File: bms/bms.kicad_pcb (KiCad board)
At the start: 8 copper layers, 60 x 60 mm, 46 parts, among them J2 3S pack power + cell-tap harn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, Q11 CSD18540Q5B reverse-pack FET A, Q12 CSD18540Q5B reverse-pack FET B, Q701 BSS138 pack protector latch r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, Q703 CSD18540Q5B BQ77915 discharge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, Q704 CSD18540Q5B BQ77915 charge FET, U11 LTC4368IMS-1 bidirectional pa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, U719 BQ7791500PWR autonomous 3S pr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

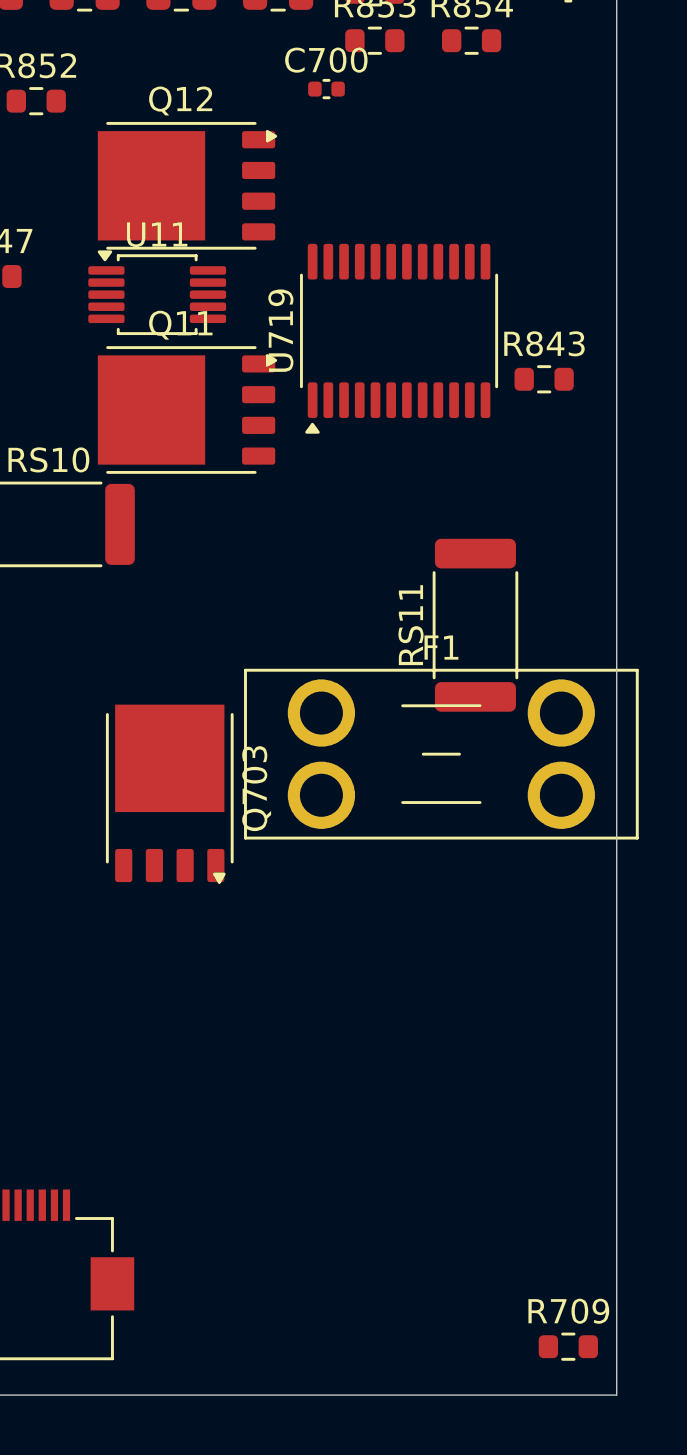
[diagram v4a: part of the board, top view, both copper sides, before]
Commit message: BMS 4-layer + test points + staged bring-up plan
- bms stackup converted from the 8-layer MCP default to a 4-copper
  JLC04161H-style build (1oz, ~1.6mm); In1/In2 are solid FG_VSS return
  planes, pads solid-connected, 2 fills, DRC 0 shorts/clearance/drill
- 16 test points (TPB1-16): every pack rail, protector gate/common,
  fault/retry, rails, gauge shunt sense, FG_VSS scope ground -- in the
  schematic generator AND injected on the board at searched-free spots
  (gen/add_test_points.py, idempotent, reusable per board)
- every differential pair on every board now in an impedance class
  (left USB3 -> DIFF_90, right HDMI/GbE -> DIFF_100, center refclk ->
  DIFF_100); bms pack-current path fully POWER_HI incl. bare FG_VSS
- inherit_netclasses restores rule keys unconditionally + center rules;
  release gate: relocated monolith path, per-board refill staging,
  via_dangling allowed in refill deltas while unrouted
- docs/BRINGUP_TEST_PLAN.md + 4x IPC-D-356 bare-board test netlists;
  verification/FPC_CABLE_SPEC_2026-09-02.md (Type-A cables, lengths,
  purchasing list)
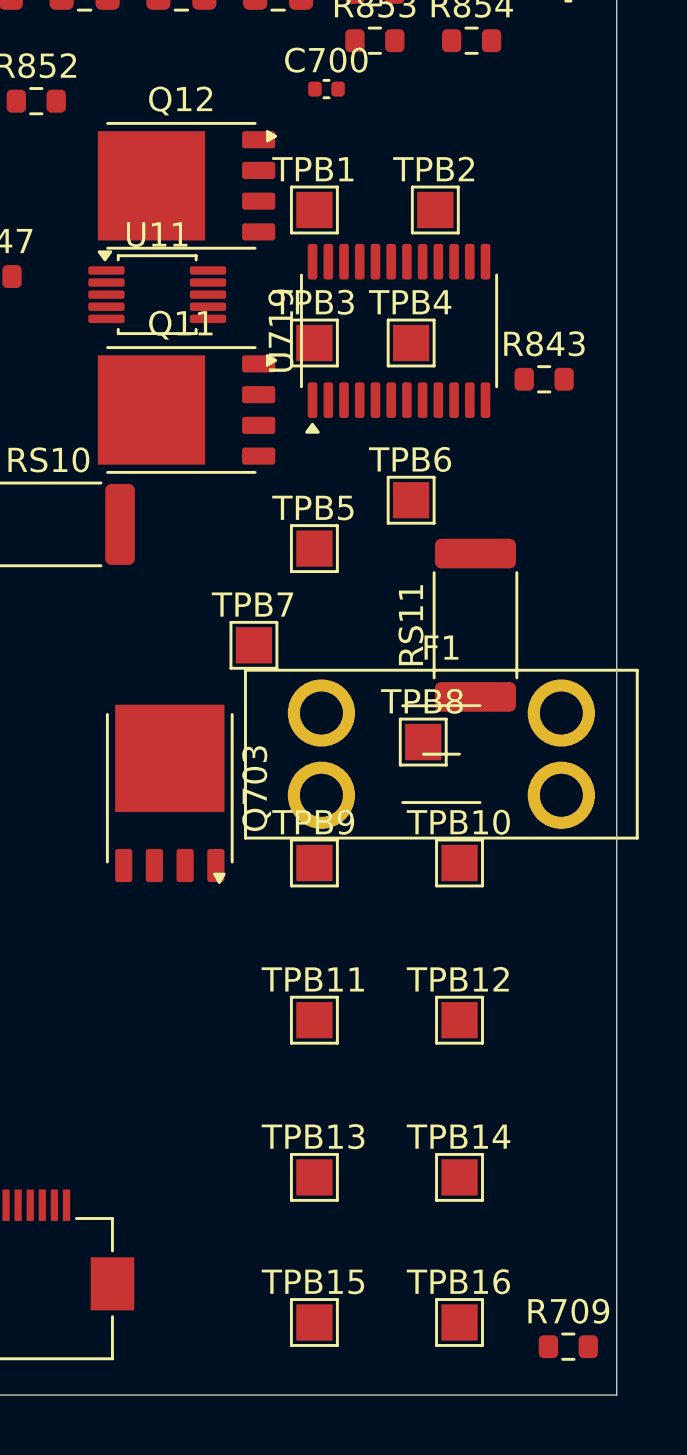
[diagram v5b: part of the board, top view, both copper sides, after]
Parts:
- added TPB1: /PACK_POS_RAW, TestPoint_Pad_1.5x1.5mm, F.Cu at (47.5, 11.0)
- added TPB10: /BMS_AVDD, TestPoint_Pad_1.5x1.5mm, F.Cu at (53.5, 38.0)
- added TPB11: /BMS_VDD, TestPoint_Pad_1.5x1.5mm, F.Cu at (47.5, 44.5)
- added TPB12: /BMS_SRP, TestPoint_Pad_1.5x1.5mm, F.Cu at (53.5, 44.5)
- added TPB13: /BMS_SRN, TestPoint_Pad_1.5x1.5mm, F.Cu at (47.5, 51.0)
- added TPB14: /BMS_PRES, TestPoint_Pad_1.5x1.5mm, F.Cu at (53.5, 51.0)
- added TPB15: /BMS_LD, TestPoint_Pad_1.5x1.5mm, F.Cu at (47.5, 57.0)
- added TPB16: FG_VSS, TestPoint_Pad_1.5x1.5mm, F.Cu at (53.5, 57.0)
- added TPB2: /BAT_PROT_VIN, TestPoint_Pad_1.5x1.5mm, F.Cu at (52.5, 11.0)
- added TPB3: /PACK_POS_FUSED, TestPoint_Pad_1.5x1.5mm, F.Cu at (47.5, 16.5)
- added TPB4: /BAT_PROT_FET_COMMON, TestPoint_Pad_1.5x1.5mm, F.Cu at (51.5, 16.5)
- added TPB5: /BAT_PROT_GATE, TestPoint_Pad_1.5x1.5mm, F.Cu at (47.5, 25.0)
- added TPB6: /BAT_PROT_CGATE, TestPoint_Pad_1.5x1.5mm, F.Cu at (51.5, 23.0)
- added TPB7: /PACK_FAULT_N, TestPoint_Pad_1.5x1.5mm, F.Cu at (45.0, 29.0)
- added TPB8: /PACK_RETRY_PULSE, TestPoint_Pad_1.5x1.5mm, F.Cu at (52.0, 33.0)
- added TPB9: /MCU_3V3, TestPoint_Pad_1.5x1.5mm, F.Cu at (47.5, 38.0)
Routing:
- added copper zone on In1.Cu, net FG_VSS
- added copper zone on In2.Cu, net FG_VSS

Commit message: finish the bms routing
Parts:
- TPB1: value /PACK_POS_RAW -> PACK_POS_RAW
- TPB10: value /BMS_AVDD -> BMS_AVDD
- TPB11: value /BMS_VDD -> BMS_VDD
- TPB12: value /BMS_SRP -> BMS_SRP
- TPB13: value /BMS_SRN -> BMS_SRN
- TPB14: value /BMS_PRES -> BMS_PRES
- TPB15: value /BMS_LD -> BMS_LD
- TPB2: value /BAT_PROT_VIN -> BAT_PROT_VIN
- TPB3: value /PACK_POS_FUSED -> PACK_POS_FUSED
- TPB4: value /BAT_PROT_FET_COMMON -> BAT_PROT_FET_COMMON
- TPB5: value /BAT_PROT_GATE -> BAT_PROT_GATE
- TPB6: value /BAT_PROT_CGATE -> BAT_PROT_CGATE
- TPB7: value /PACK_FAULT_N -> PACK_FAULT_N
- TPB8: value /PACK_RETRY_PULSE -> PACK_RETRY_PULSE
- TPB9: value /MCU_3V3 -> MCU_3V3
- moved R702 159.4 mm to (142.9, 76.5), turned to 90 degrees
- moved J2 155.2 mm to (149.9, 80.7)
- moved Q704 150.8 mm to (152.2, 67.4), turned to -90 degrees
- moved R845 149.0 mm to (126.7, 88.2)
- moved R842 145.2 mm to (137.0, 86.5)
- moved R707 142.2 mm to (146.2, 73.0), turned to 90 degrees
- moved R844 141.8 mm to (119.2, 83.8), turned to 180 degrees
- moved R850 140.1 mm to (153.2, 72.4), turned to 180 degrees
- moved C840 139.8 mm to (122.0, 80.1), turned to 180 degrees
- moved Q701 138.7 mm to (143.5, 73.2), turned to 0 degrees
- moved C841 137.7 mm to (122.0, 82.1), turned to 180 degrees
- moved R708 136.4 mm to (137.6, 72.3), turned to 0 degrees
- moved C845 135.8 mm to (126.0, 77.0), turned to -90 degrees
- moved R701 135.4 mm to (141.4, 76.2), turned to 90 degrees
- moved R846 134.4 mm to (123.2, 72.2)
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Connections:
- F1 pad 2: /PACK_POS_FUSED -> /BAT_PROT_VIN
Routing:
- net /PACK_POS_RAW: track 0.00 -> 200.2 mm, vias 0 -> 7
- net /PACK_POS_FUSED: track 0.00 -> 154.2 mm, vias 0 -> 15
- net /BAT_PROT_SENSE: track 0.00 -> 151.4 mm, vias 0 -> 9
- net /BAT_PROT_VIN: track 0.00 -> 89.0 mm, vias 0 -> 5
- net /BAT_PROT_GATE: track 0.00 -> 75.9 mm, vias 0 -> 2
- net /BAT_PROT_FET_COMMON: track 0.00 -> 74.5 mm, vias 0 -> 6
- net /PACK_NEG_RAW: track 0.00 -> 60.5 mm, vias 0 -> 11
- net FG_VSS: track 0.00 -> 47.6 mm, vias 0 -> 237
- net /CELL2_TAP: track 0.00 -> 40.4 mm, vias 0 -> 1
- net /PACK_FAULT_N: track 0.00 -> 33.1 mm
- net /BMS_FET_COMMON: track 0.00 -> 32.1 mm
- net /BMS_VC1: track 0.00 -> 31.3 mm, vias 0 -> 2
- net /BMS_CHG_GATE: track 0.00 -> 28.0 mm, vias 0 -> 2
- net /BMS_SRP: track 0.00 -> 26.4 mm, vias 0 -> 2
- net /BMS_SRN: track 0.00 -> 24.7 mm, vias 0 -> 2
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- added copper zone on In2.Cu, net /BAT_PROT_FET_COMMON
- added copper zone on B.Cu, net /BAT_PROT_SENSE
- added copper zone on In1.Cu, net /BAT_PROT_VIN
- added copper zone on F.Cu, net /BMS_FET_COMMON
- added copper zone on B.Cu, net /PACK_NEG_RAW
- added copper zone on F.Cu, net /PACK_NEG_RAW
- added copper zone on In2.Cu, net /PACK_NEG_RAW
- added copper zone on In1.Cu, net /PACK_POS_FUSED
- added copper zone on B.Cu, net /PACK_POS_RAW
- added copper zone on In1.Cu, net /PACK_POS_RAW
- added copper zone on B.Cu, net FG_VSS
- added copper zone on F.Cu, net FG_VSS
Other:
- board size 60 x 60 mm -> 61.9 x 30.3 mm
- copper layers 8 -> 4

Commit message: get the main boards ready for routing
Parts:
- TPB1, TPB10, TPB11, TPB12, TPB13, TPB14, TPB15, TPB16, TPB2, TPB3, TPB4, TPB5, TPB6, TPB7, TPB8, TPB9: footprint TestPoint_Pad_1.5x1.5mm -> TestPoint:TestPoint_Pad_1.5x1.5mm
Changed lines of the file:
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@@
 		)
 	)
-	(footprint "TestPoint_Pad_1.5x1.5mm"
+	(footprint "TestPoint:TestPoint_Pad_1.5x1.5mm"
 		(layer "F.Cu")
 		(at 128.05 77.8 180)
@@
 		)
 	)
-	(footprint "TestPoint_Pad_1.5x1.5mm"
+	(footprint "TestPoint:TestPoint_Pad_1.5x1.5mm"
 		(layer "F.Cu")
 		(at 130.55 77.8 180)
@@
 		(embedded_fonts no)
 	)
-	(footprint "TestPoint_Pad_1.5x1.5mm"
+	(footprint "TestPoint:TestPoint_Pad_1.5x1.5mm"
 		(layer "F.Cu")
 		(at 128.5 75.3 180)
@@
 		)
 	)
-	(footprint "TestPoint_Pad_1.5x1.5mm"
+	(footprint "TestPoint:TestPoint_Pad_1.5x1.5mm"
 		(layer "F.Cu")
 		(at 115.85 83.85 180)
@@
 		(embedded_fonts no)
 	)
-	(footprint "TestPoint_Pad_1.5x1.5mm"
+	(footprint "TestPoint:TestPoint_Pad_1.5x1.5mm"
 		(layer "F.Cu")
 		(at 149.25 72.7 180)
@@
 		)
 	)
-	(footprint "TestPoint_Pad_1.5x1.5mm"
+	(footprint "TestPoint:TestPoint_Pad_1.5x1.5mm"
 		(layer "F.Cu")
 		(at 123.5 74.15 180)
@@
 		)
 	)
-	(footprint "TestPoint_Pad_1.5x1.5mm"
+	(footprint "TestPoint:TestPoint_Pad_1.5x1.5mm"
 		(layer "F.Cu")
 		(at 131 72.8 180)
@@
 		)
 	)
-	(footprint "TestPoint_Pad_1.5x1.5mm"
+	(footprint "TestPoint:TestPoint_Pad_1.5x1.5mm"
 		(layer "F.Cu")
 		(at 126 74.2 180)
@@
 		)
 	)
-	(footprint "TestPoint_Pad_1.5x1.5mm"
+	(footprint "TestPoint:TestPoint_Pad_1.5x1.5mm"
 		(layer "F.Cu")
 		(at 152.2 75.55 180)
@@
 		)
 	)
-	(footprint "TestPoint_Pad_1.5x1.5mm"
+	(footprint "TestPoint:TestPoint_Pad_1.5x1.5mm"
 		(layer "F.Cu")
 		(at 140.35 72.85 180)
@@
 		(embedded_fonts no)
 	)
-	(footprint "TestPoint_Pad_1.5x1.5mm"
+	(footprint "TestPoint:TestPoint_Pad_1.5x1.5mm"
 		(layer "F.Cu")
 		(at 131 75.3 180)
@@
 		)
 	)
-	(footprint "TestPoint_Pad_1.5x1.5mm"
+	(footprint "TestPoint:TestPoint_Pad_1.5x1.5mm"
 		(layer "F.Cu")
 		(at 128.5 72.8 180)
@@
 		)
 		(property "Value" "1k 1% BQ77915 VDD filter"
-			(at 0 1.43 -180)
+			(at 0 1.43 180)
 			(layer "F.Fab")
 			(effects
@@
 		)
 		(property "Datasheet" ""
-			(at 0 0 -180)
+			(at 0 0 180)
 			(layer "F.Fab")
 			(hide yes)
@@
 		)
 		(property "Description" ""
-			(at 0 0 -180)
+			(at 0 0 180)
 			(layer "F.Fab")
 			(hide yes)
@@
 		)
 		(property "KiLib_Generator" "SMD_2terminal_chip_molded"
-			(at 0 0 -180)
+			(at 0 0 180)
 			(layer "F.SilkS")
 			(hide yes)
@@
 		(embedded_fonts no)
 	)
-	(footprint "TestPoint_Pad_1.5x1.5mm"
+	(footprint "TestPoint:TestPoint_Pad_1.5x1.5mm"
 		(layer "F.Cu")
 		(at 115.3 72.65 180)
@@
 		)
 	)
-	(footprint "TestPoint_Pad_1.5x1.5mm"
+	(footprint "TestPoint:TestPoint_Pad_1.5x1.5mm"
 		(layer "F.Cu")
 		(at 149.7 75.2 180)
@@
 		)
 	)
-	(footprint "TestPoint_Pad_1.5x1.5mm"
+	(footprint "TestPoint:TestPoint_Pad_1.5x1.5mm"
 		(layer "F.Cu")
 		(at 133.05 77.8 180)
@@
 		)
 	)
-	(footprint "TestPoint_Pad_1.5x1.5mm"
+	(footprint "TestPoint:TestPoint_Pad_1.5x1.5mm"
 		(layer "F.Cu")
 		(at 134.85 72.85 180)

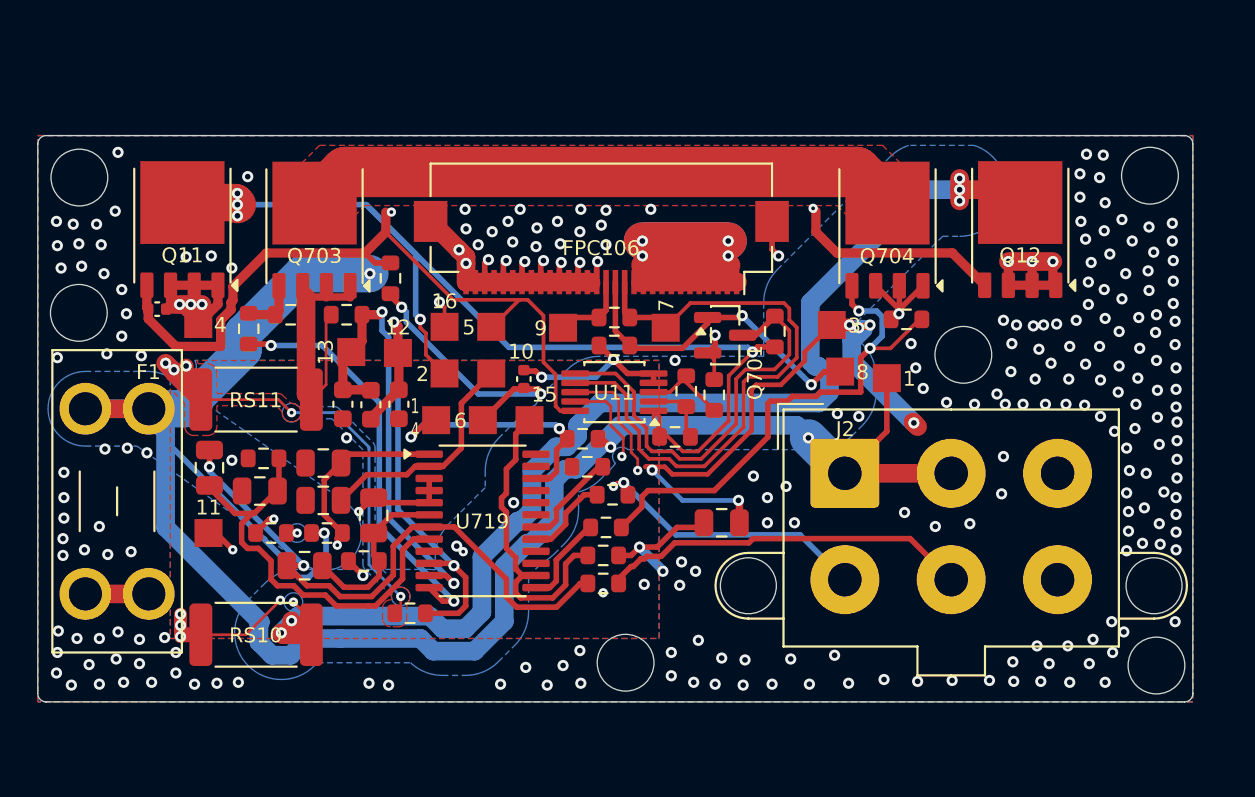
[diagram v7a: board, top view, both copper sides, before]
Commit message: route more of the bms
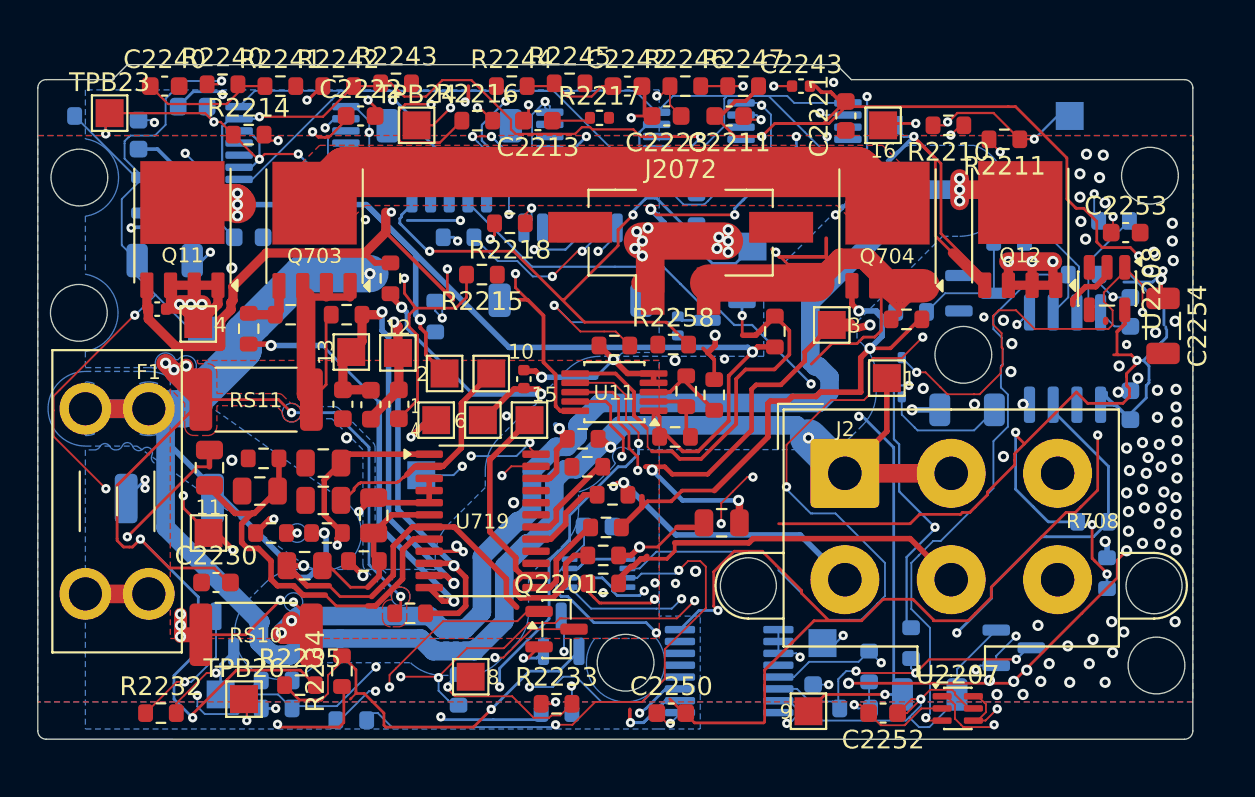
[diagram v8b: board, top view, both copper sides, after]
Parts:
- removed FPC106: FH12-30S-0.5SH (FPC-3), Connector_FFC-FPC:Hirose_FH12-30S-0.5SH_1x30-1MP_P0.50mm_Horizontal
- added C2200: 100n 50V thermal regulator input, Capacitor_SMD:C_0603_1608Metric, B.Cu at (112.1, 62.5)
- added C2201: 10u 50V thermal bias; require Ceff >=2u, Capacitor_SMD:C_1206_3216Metric, B.Cu at (113.5, 69.2)
- added C2211: 10n 50V NTC sense filter, Capacitor_SMD:C_0603_1608Metric, F.Cu at (143.8, 61.5)
- added C2212: 10n 50V NTC sense filter, Capacitor_SMD:C_0603_1608Metric, B.Cu at (115.0, 61.0)
- added C2213: 10n 50V NTC sense filter, Capacitor_SMD:C_0603_1608Metric, F.Cu at (133.5, 61.8)
- added C2221: 100n 50V comparator supply, Capacitor_SMD:C_0603_1608Metric, F.Cu at (150.0, 61.5)
- added C2222: 100n 50V comparator supply, Capacitor_SMD:C_0603_1608Metric, F.Cu at (124.0, 61.5)
- added C2223: 100n 50V comparator supply, Capacitor_SMD:C_0603_1608Metric, F.Cu at (140.4, 61.5)
- added C2230: 100n 50V thermal supervisor supply, Capacitor_SMD:C_0603_1608Metric, F.Cu at (116.2, 86.5)
- added C2231: 100n 50V thermal buffer supply, Capacitor_SMD:C_0603_1608Metric, B.Cu at (136.8, 83.5)
- added C2240: 10n 50V thermal reference filter, Capacitor_SMD:C_0603_1608Metric, F.Cu at (113.5, 59.9)
- added C2241: 10n 50V thermal reference filter, Capacitor_SMD:C_0603_1608Metric, B.Cu at (118.0, 68.0)
- added C2242: 10n 50V thermal reference filter, Capacitor_SMD:C_0603_1608Metric, F.Cu at (138.3, 59.9)
- added C2243: 10n 50V thermal reference filter, Capacitor_SMD:C_0402_1005Metric, F.Cu at (147.6, 59.9)
- added C2250: 100n 50V raw isolator supply, Capacitor_SMD:C_0603_1608Metric, F.Cu at (140.7, 93.5)
- added C2251: 100n 50V control-island isolator supply, Capacitor_SMD:C_0603_1608Metric, B.Cu at (148.2, 92.8)
- added C2252: 100n 50V control fault-buffer supply, Capacitor_SMD:C_0603_1608Metric, F.Cu at (152.0, 93.5)
- added C2253: 100n 50V protected control regulator input, Capacitor_SMD:C_0603_1608Metric, F.Cu at (165.0, 67.8)
- added C2254: 10u 50V protected local bias; Ceff >=2u, Capacitor_SMD:C_1206_3216Metric, F.Cu at (167.0, 72.8)
- added C2255: 100n 50V protected transceiver supply, Capacitor_SMD:C_0603_1608Metric, B.Cu at (165.2, 77.0)
- added C2256: 100n 50V control transceiver supply, Capacitor_SMD:C_0603_1608Metric, B.Cu at (165.2, 72.0)
- added D2200: BAT54WS protected control reverse-input block, Diode_SMD:D_SOD-323, B.Cu at (153.0, 75.5)
- added D2201: BAT54S control-island pin clamps, Package_TO_SOT_SMD:SOT-23, B.Cu at (157.0, 71.0)
- added D2202: BAT54S control-island pin clamps, Package_TO_SOT_SMD:SOT-23, B.Cu at (159.0, 90.0)
- added J2072: protected pack power, Connector_Molex:Molex_Micro-Fit_3.0_43650-0224_1x02-1MP_P3.00mm_Vertical, F.Cu at (141.2, 67.8)
- added J2074: isolated bms control, Connector_JST:JST_SH_SM05B-SRSS-TB_1x05-1MP_P1.00mm_Horizontal, B.Cu at (128.8, 63.9)
- added J2200: three cell probes: paired 1/2, 3/4, 5/6, Connector_JST:JST_SH_SM06B-SRSS-TB_1x06-1MP_P1.00mm_Horizontal, B.Cu at (135.2, 69.5)
- added Q2200: BSS138 CHG thermal CTR pull-down, Package_TO_SOT_SMD:SOT-23, B.Cu at (134.8, 89.2)
- added Q2201: BSS138 DSG thermal CTR pull-down, Package_TO_SOT_SMD:SOT-23, F.Cu at (134.5, 89.0)
- added R2200: 1k 1% 0.75W raw thermal supply limiter, Resistor_SMD:R_2010_5025Metric, B.Cu at (113.8, 82.0)
- added R2201: 9.53k 0.1% 25ppm thermal bias fault bleed, Resistor_SMD:R_0603_1608Metric, B.Cu at (129.2, 92.2)
- added R2210: 100k 0.1% 25ppm cell NTC pull-up, Resistor_SMD:R_0603_1608Metric, F.Cu at (155.5, 62.0)
- added R2211: 10k 0.1% 25ppm NTC sense-lead limit, Resistor_SMD:R_0603_1608Metric, F.Cu at (158.5, 62.8)
- added R2212: 10k 0.1% 25ppm NTC return-lead limit, Resistor_SMD:R_0603_1608Metric, B.Cu at (129.2, 68.0)
- added R2213: 100k 0.1% 25ppm cell NTC pull-up, Resistor_SMD:R_0603_1608Metric, B.Cu at (109.5, 61.5)
- added R2214: 10k 0.1% 25ppm NTC sense-lead limit, Resistor_SMD:R_0603_1608Metric, F.Cu at (118.0, 62.5)
- added R2215: 10k 0.1% 25ppm NTC return-lead limit, Resistor_SMD:R_0603_1608Metric, F.Cu at (130.5, 70.0)
- added R2216: 100k 0.1% 25ppm cell NTC pull-up, Resistor_SMD:R_0603_1608Metric, F.Cu at (130.2, 61.8)
- added R2217: 10k 0.1% 25ppm NTC sense-lead limit, Resistor_SMD:R_0402_1005Metric, F.Cu at (136.8, 61.6)
- added R2218: 10k 0.1% 25ppm NTC return-lead limit, Resistor_SMD:R_0603_1608Metric, F.Cu at (132.0, 67.2)
- added R2230: 100k thermal charge-health pull-up, Resistor_SMD:R_0603_1608Metric, B.Cu at (142.0, 66.5)
- added R2231: 100k thermal discharge-health pull-up, Resistor_SMD:R_0603_1608Metric, B.Cu at (128.0, 72.2)
- added R2232: 100k thermal-ready pull-up, Resistor_SMD:R_0603_1608Metric, F.Cu at (113.3, 93.5)
- added R2233: 1M thermal-ready default-low, Resistor_SMD:R_0603_1608Metric, F.Cu at (134.5, 93.0)
- added R2234: 1k thermal CTR gate series, Resistor_SMD:R_0603_1608Metric, F.Cu at (123.0, 91.2)
- added R2235: 100k thermal CTR gate default-off, Resistor_SMD:R_0603_1608Metric, F.Cu at (120.8, 92.0)
- added R2236: 470k 0.1% 25ppm CTR fault pull-up, Resistor_SMD:R_0603_1608Metric, B.Cu at (134.5, 93.5)
- added R2237: 1k thermal CTR gate series, Resistor_SMD:R_0603_1608Metric, B.Cu at (123.5, 93.9)
- added R2238: 100k thermal CTR gate default-off, Resistor_SMD:R_0603_1608Metric, B.Cu at (119.5, 91.8)
- added R2239: 470k 0.1% 25ppm CTR fault pull-up, Resistor_SMD:R_0603_1608Metric, B.Cu at (119.5, 93.2)
- added R2240: 243k 0.1% 25ppm CHG_COLD top, Resistor_SMD:R_0603_1608Metric, F.Cu at (116.6, 59.8)
- added R2241: 499k 0.1% 25ppm thermal reference bottom, Resistor_SMD:R_0603_1608Metric, F.Cu at (119.7, 59.9)
- added R2242: 634k 0.1% 25ppm CHG_HOT top, Resistor_SMD:R_0603_1608Metric, F.Cu at (122.8, 59.9)
- added R2243: 499k 0.1% 25ppm thermal reference bottom, Resistor_SMD:R_0603_1608Metric, F.Cu at (125.9, 59.8)
- added R2244: 147k 0.1% 25ppm DSG_COLD top, Resistor_SMD:R_0603_1608Metric, F.Cu at (132.1, 59.9)
- added R2245: 499k 0.1% 25ppm thermal reference bottom, Resistor_SMD:R_0603_1608Metric, F.Cu at (135.2, 59.8)
- added R2246: 845k 0.1% 25ppm DSG_HOT top, Resistor_SMD:R_0603_1608Metric, F.Cu at (141.4, 59.9)
- added R2247: 499k 0.1% 25ppm thermal reference bottom, Resistor_SMD:R_0603_1608Metric, F.Cu at (144.5, 59.9)
- added R2250: 100k isolated discharge-health default-low, Resistor_SMD:R_0603_1608Metric, B.Cu at (151.2, 91.0)
- added R2251: 100k isolated charge-permit default-low, Resistor_SMD:R_0603_1608Metric, B.Cu at (150.5, 93.2)
- added R2252: 2.49k 1% 0.25W protected control supply limiter, Resistor_SMD:R_1206_3216Metric, B.Cu at (156.5, 77.2)
- added R2253: 30.1k 0.1% protected bias minimum load, Resistor_SMD:R_0603_1608Metric, B.Cu at (164.0, 86.0)
- added R2254: 1k local retry gate series, Resistor_SMD:R_0402_1005Metric, B.Cu at (141.0, 72.8)
- added R2255: 100k isolated LTC-health default-low, Resistor_SMD:R_0603_1608Metric, B.Cu at (162.8, 70.0)
- added R2256: 3.3k control fault pull-up, Resistor_SMD:R_0603_1608Metric, B.Cu at (164.4, 67.1)
- added R2257: 100R 1% 0.25W control-island current limiter, Resistor_SMD:R_1206_3216Metric, B.Cu at (154.5, 92.5)
- added R2258: 4.7k fault interface current limit, Resistor_SMD:R_0603_1608Metric, F.Cu at (140.8, 73.8)
- added R2259: 4.7k retry interface current limit, Resistor_SMD:R_0603_1608Metric, B.Cu at (153.5, 72.0)
- added R2264: 100k retry input default-low, Resistor_SMD:R_0603_1608Metric, B.Cu at (158.8, 68.2)
- added R2265: 4.7k charge-permit interface current limit, Resistor_SMD:R_0603_1608Metric, B.Cu at (153.5, 89.8)
- added TPB20: THERM_3V3, TestPoint:TestPoint_Pad_1.5x1.5mm, B.Cu at (115.5, 73.0)
- added TPB21: THERM_READY, TestPoint:TestPoint_Pad_1.5x1.5mm, B.Cu at (116.5, 92.5)
- added TPB22: THERM_SENSE_1, TestPoint:TestPoint_Pad_1.5x1.5mm, B.Cu at (162.0, 61.5)
- added TPB23: THERM_SENSE_2, TestPoint:TestPoint_Pad_1.5x1.5mm, F.Cu at (110.5, 61.4)
- added TPB24: THERM_SENSE_3, TestPoint:TestPoint_Pad_1.5x1.5mm, F.Cu at (127.0, 62.0)
- added TPB25: BMS_CTRC, TestPoint:TestPoint_Pad_1.5x1.5mm, B.Cu at (127.2, 80.8)
- added TPB26: BMS_CTRD, TestPoint:TestPoint_Pad_1.5x1.5mm, F.Cu at (117.8, 92.8)
- added TPB27: PACK_CHG_TEMP_OK, TestPoint:TestPoint_Pad_1.5x1.5mm, B.Cu at (148.8, 89.8)
- added U2200: TPS70933DBVR raw-pack thermal bias, Package_TO_SOT_SMD:SOT-23-5, B.Cu at (113.5, 65.8)
- added U2201: TLV1864PWR cell 1 thermal windows, Package_SO:TSSOP-14_4.4x5mm_P0.65mm, B.Cu at (147.2, 62.8)
- added U2202: TLV1864PWR cell 2 thermal windows, Package_SO:TSSOP-14_4.4x5mm_P0.65mm, B.Cu at (120.3, 63.0)
- added U2203: TLV1864PWR cell 3 thermal windows, Package_SO:TSSOP-14_4.4x5mm_P0.65mm, B.Cu at (137.0, 63.2)
- added U2204: TLV803EA29RDBZR thermal startup hold, Package_TO_SOT_SMD:SOT-23, B.Cu at (116.2, 89.2)
- added U2205: SN74AUP2G126DCUR thermal startup gate, ducktop2:TI_DCU0008A_VSSOP8, B.Cu at (136.8, 86.0)
- added U2206: ISO7041FDBQR separate charge/discharge permits; default low, Package_SO:QSOP-16_3.9x4.9mm_P0.635mm, B.Cu at (143.8, 91.2)
- added U2207: SN74AUP2G07DCKR thermal and LTC fault wired-OR, Package_TO_SOT_SMD:SOT-363_SC-70-6, F.Cu at (156.0, 93.2)
- added U2208: TPS70933DBVR protected-side local bias, Package_TO_SOT_SMD:SOT-23-5, F.Cu at (164.0, 70.8)
- added U2209: ISO7021FDR LTC fault and retry isolation, Package_SO:SOIC-8_3.9x4.9mm_P1.27mm, B.Cu at (161.8, 74.5)
- Q701, TPB7: moved to B.Cu
- R708: value 10k pack FAULT pull-up -> 100k protected-side LTC fault pull-up; moved to B.Cu
- TPB5: footprint TestPoint:TestPoint_Pad_1.5x1.5mm -> TestPoint:TestPoint_Pad_1.0x1.0mm; moved to B.Cu
- moved R708 27.9 mm to (163.2, 83.2)
- moved TPB16 25.9 mm to (152.0, 62.0), turned to 0 degrees
- moved TPB8 25.7 mm to (129.9, 91.5)
- moved TPB9 24.4 mm to (148.0, 93.4)
- moved TPB5 24.1 mm to (152.6, 62.0), turned to 0 degrees
- moved TPB7 6.37 mm to (145.0, 68.5), turned to 0 degrees
- moved Q701 1.75 mm to (143.5, 71.5)
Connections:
- Q701 pad 1: /PACK_RETRY_PULSE -> /PACK_RETRY_LOCAL_GATE
- R708 pad 1: /MCU_3V3 -> /PROT_CTRL_3V3
- R708 pad 2: /PACK_FAULT_N -> /BMS_PROTECT_FAULT_N
- R709 pad 1: /PACK_RETRY_PULSE -> /PACK_RETRY_LOCAL_GATE
- U11 pad 7: /PACK_FAULT_N -> /BMS_PROTECT_FAULT_N
- U719 pad 15: unconnected-(U719-LPWR-Pad15) -> (no net)
- U719 pad 19: unconnected-(U719-VTB-Pad19) -> (no net)
- U719 pad 21: unconnected-(U719-CBO-Pad21) -> (no net)
- U719 pad 23: /PACK_NEG_RAW -> /BMS_CTRC
- U719 pad 24: /PACK_NEG_RAW -> /BMS_CTRD
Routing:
- net /PACK_NEG_RAW: track 60.5 -> 356.3 mm, vias 11 -> 33
- net /THERM_3V3: track 0.00 -> 179.9 mm, vias 0 -> 14
- net /THERM_CHG_HEALTH: track 0.00 -> 131.7 mm, vias 0 -> 3
- net /THERM_DSG_HEALTH: track 0.00 -> 118.9 mm, vias 0 -> 11
- net FG_VSS: track 47.6 -> 135.2 mm, vias 237 -> 84
- net /BMS_PROTECT_FAULT_N: track 0.00 -> 68.4 mm, vias 0 -> 3
- net /BAT_PROT_GATE: track 75.9 -> 143.4 mm, vias 2 -> 6
- net /CTRL_GND: track 0.00 -> 66.9 mm, vias 0 -> 9
- net /PROT_CTRL_3V3: track 0.00 -> 64.6 mm, vias 0 -> 6
- net /MCU_3V3: track 4.21 -> 67.9 mm, vias 0 -> 3
- net /THERM_CHG_HOT_REF: track 0.00 -> 53.0 mm, vias 0 -> 3
- net /PACK_CHG_TEMP_OK: track 0.00 -> 52.4 mm, vias 0 -> 4
- net /THERM_DSG_HOT_REF: track 0.00 -> 51.1 mm, vias 0 -> 4
- net /BMS_VC1: track 31.3 -> 78.9 mm, vias 2 -> 3
- net /BMS_CTRD: track 0.00 -> 47.6 mm, vias 0 -> 5
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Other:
- board size 61.9 x 30.3 mm -> 61.9 x 36.1 mm
